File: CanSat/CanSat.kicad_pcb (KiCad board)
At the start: 2 copper layers, 7 parts, among them J1 MPU_XH2.54_M, J2 MPU_XH2.54_H, U1 ESP32_DevKit_V1, U2 LoRa Ra-02, U3 NEO6MV2 GPS, U4 MPU-6050, U5 BME280

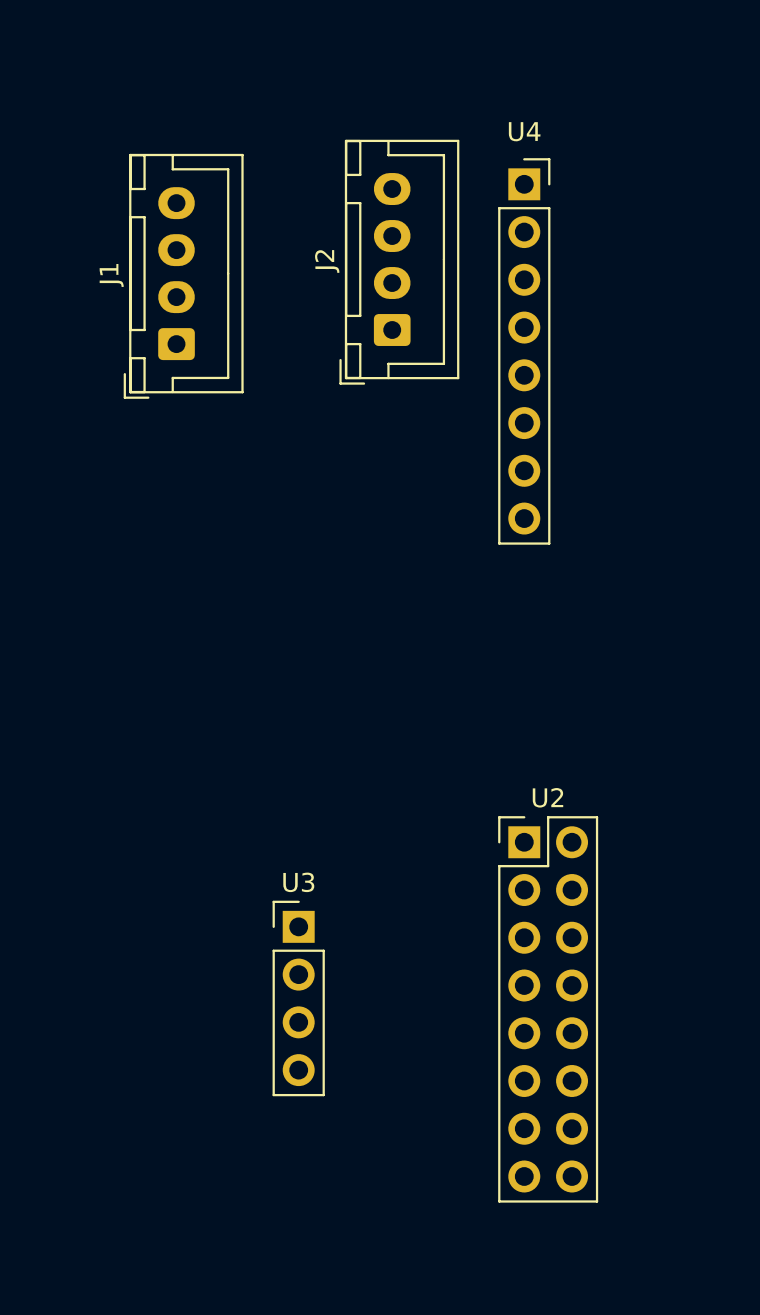
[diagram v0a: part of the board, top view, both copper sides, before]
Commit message: Updated schematic and added footprints
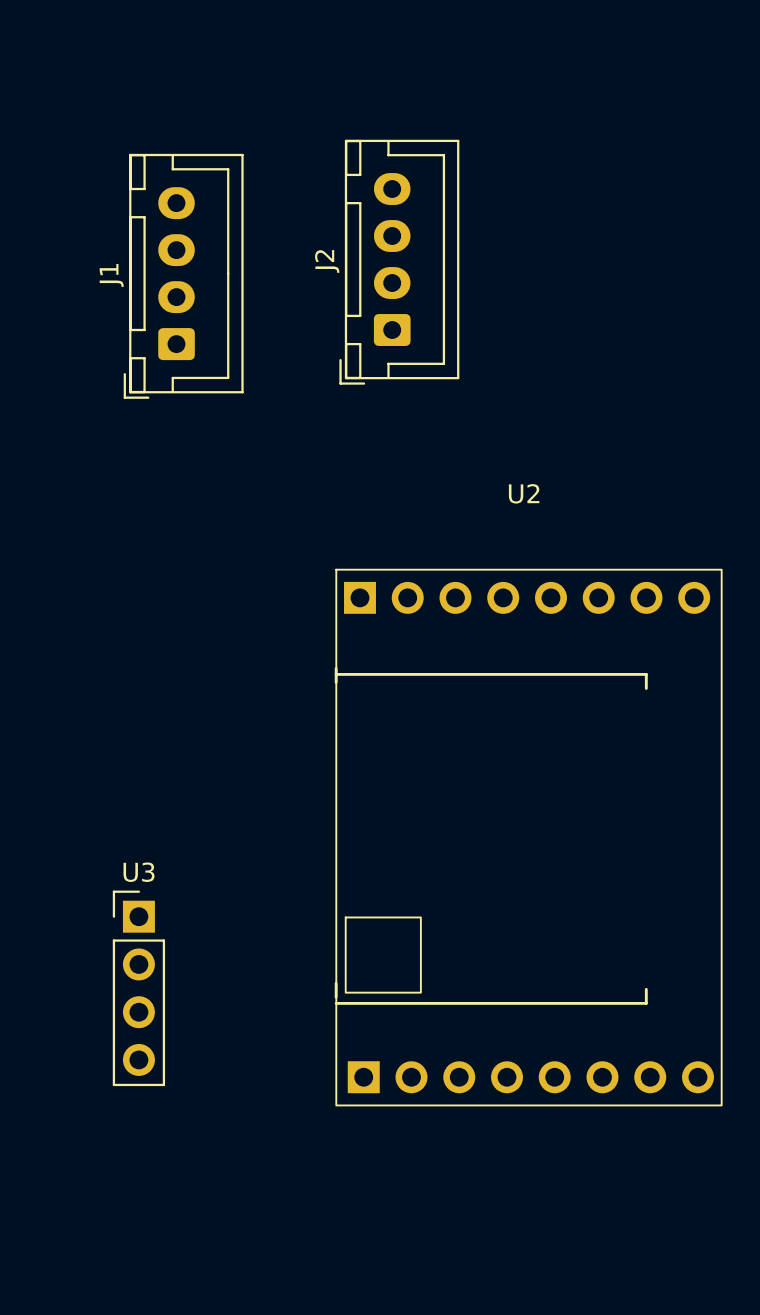
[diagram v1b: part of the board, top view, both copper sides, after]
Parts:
- removed U4: MPU-6050, Connector_PinSocket_2.54mm:PinSocket_1x08_P2.54mm_Vertical
- U2: footprint Connector_PinHeader_2.54mm:PinHeader_2x08_P2.54mm_Vertical -> MyLibrary:LoRa Ra-02
- moved U3 8.52 mm to (244.0, 120.0)

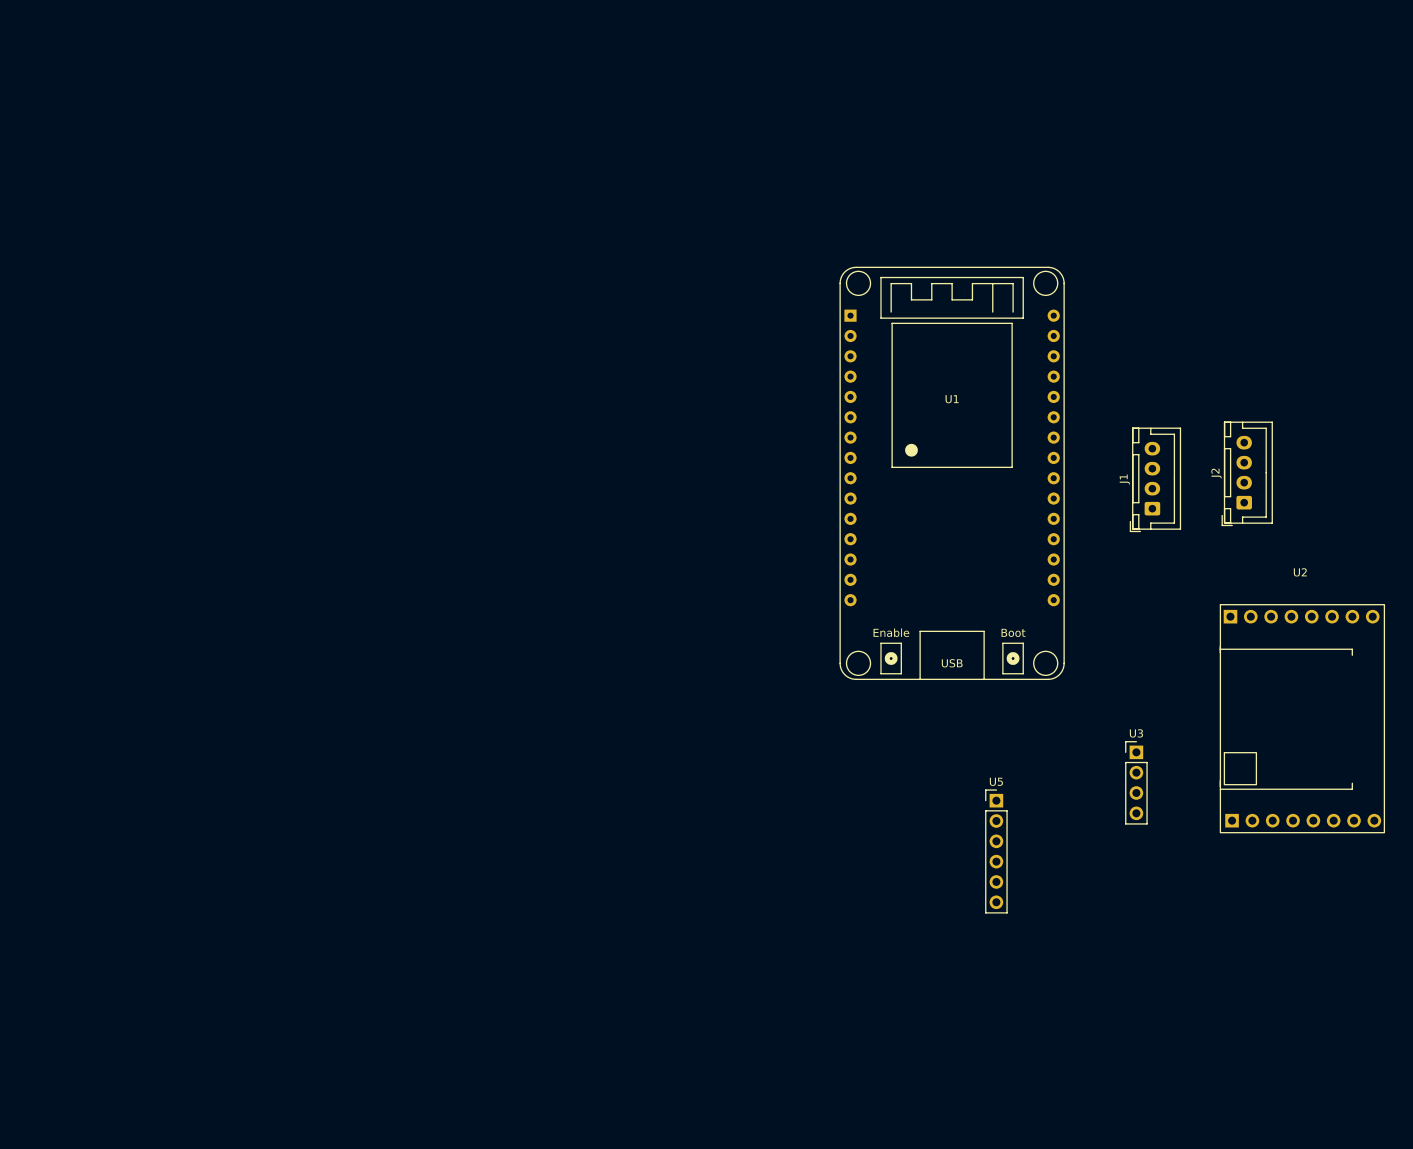
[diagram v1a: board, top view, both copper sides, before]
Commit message: Change schemes and footprints
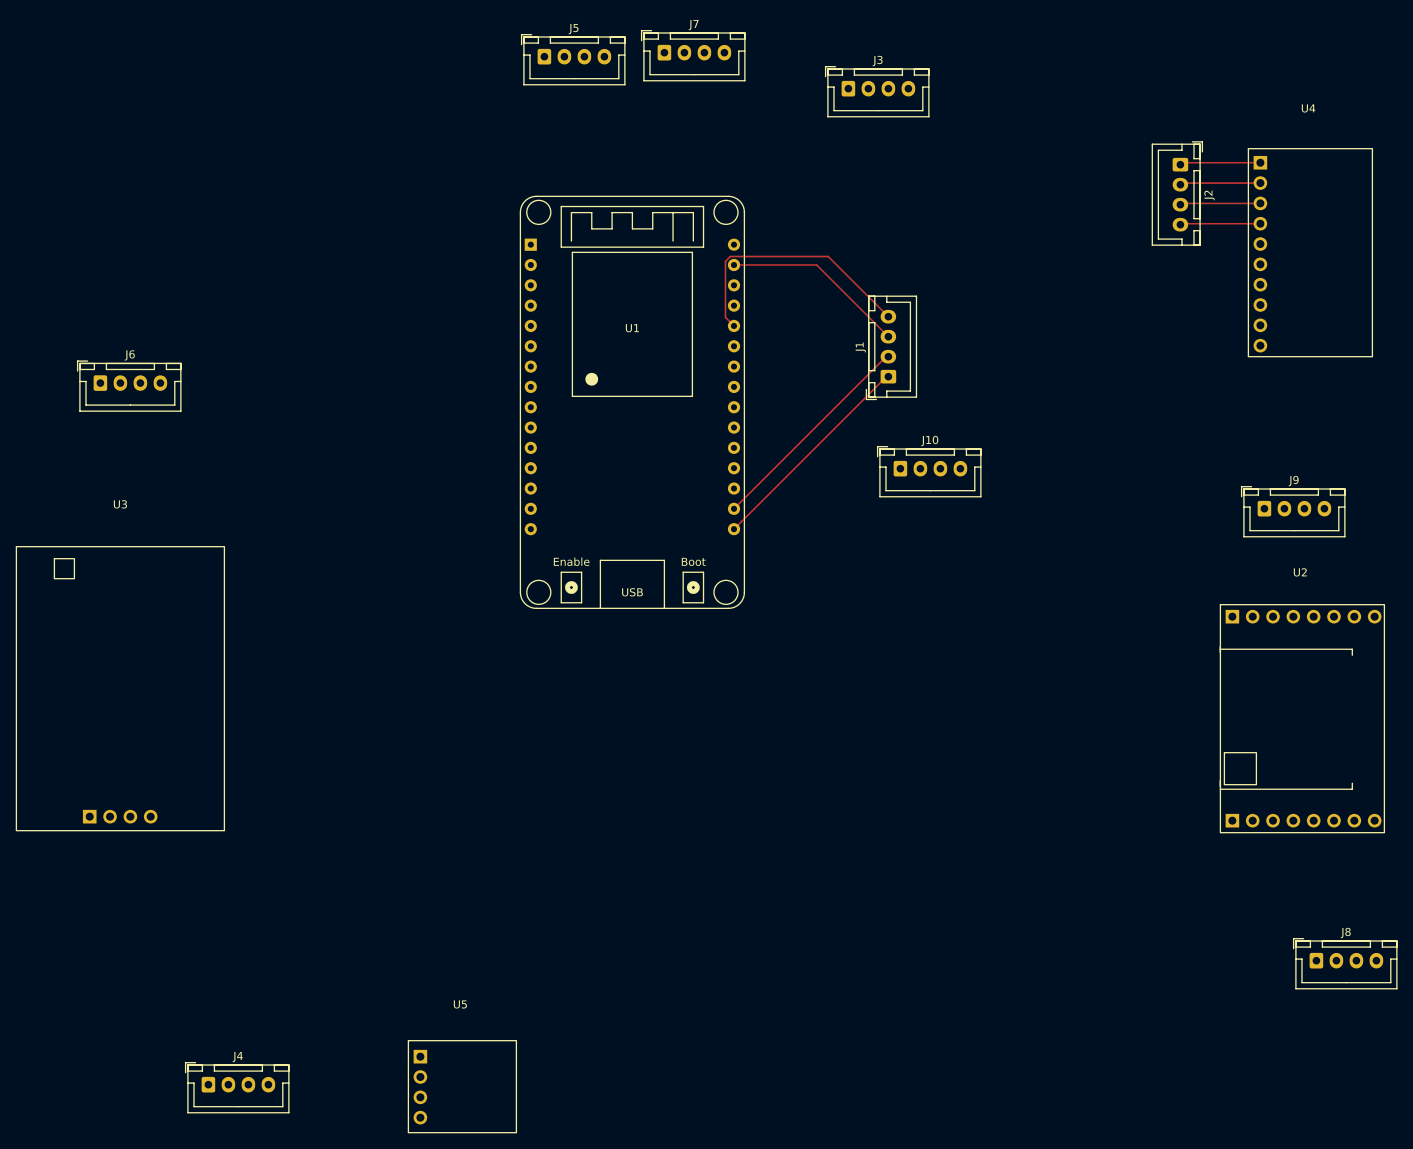
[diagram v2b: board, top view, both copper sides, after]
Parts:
- added J10: MPU_XH2.54_H, Connector_JST:JST_XH_B4B-XH-A_1x04_P2.50mm_Vertical, F.Cu at (214.5, 84.5)
- added J3: BME_XH2.54_M, Connector_JST:JST_XH_B4B-XH-A_1x04_P2.50mm_Vertical, F.Cu at (208.0, 37.0)
- added J4: BME_XH2.54_H, Connector_JST:JST_XH_B4B-XH-A_1x04_P2.50mm_Vertical, F.Cu at (128.0, 161.5)
- added J5: GPS_XH2.54_M, Connector_JST:JST_XH_B4B-XH-A_1x04_P2.50mm_Vertical, F.Cu at (170.0, 33.0)
- added J6: GPS_XH2.54_H, Connector_JST:JST_XH_B4B-XH-A_1x04_P2.50mm_Vertical, F.Cu at (114.5, 73.8)
- added J7: LoRa1_XH2.54_M, Connector_JST:JST_XH_B4B-XH-A_1x04_P2.50mm_Vertical, F.Cu at (185.0, 32.5)
- added J8: LoRa1_XH2.54_H, Connector_JST:JST_XH_B4B-XH-A_1x04_P2.50mm_Vertical, F.Cu at (266.5, 146.0)
- added J9: MPU_XH2.54_M, Connector_JST:JST_XH_B4B-XH-A_1x04_P2.50mm_Vertical, F.Cu at (260.0, 89.5)
- added U4: MPU-6500, MyLibrary:MPU-6500, F.Cu at (265.5, 57.5)
- U3: footprint Connector_PinHeader_2.54mm:PinHeader_1x04_P2.54mm_Vertical -> MyLibrary:NE06MV2 GPS
- U5: footprint Connector_PinHeader_2.54mm:PinHeader_1x06_P2.54mm_Vertical -> MyLibrary:BME280
- moved U3 127.2 mm to (117.0, 112.0)
- moved U5 76.1 mm to (159.5, 162.0)
- moved J2 43.0 mm to (249.5, 46.5), turned to -90 degrees
- moved U1 40.9 mm to (181.0, 56.5)
- moved J1 36.9 mm to (213.0, 73.0)
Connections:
- J1 pad 1: MPU.SDA -> GPS.VCC
- J1 pad 2: MPU.SCL -> GPS.GND
- J1 pad 3: MPU.GND -> BME.SCL
- J1 pad 4: MPU.VCC -> BME.SDA
- J2 pad 1: MPU.SDA -> Net-(J2-Pin_1)
- J2 pad 2: MPU.SCL -> Net-(J2-Pin_2)
- J2 pad 3: MPU.GND -> Net-(J2-Pin_3)
- J2 pad 4: MPU.VCC -> Net-(J2-Pin_4)
- U1 pad 11: unconnected-(U1-IO14-Pad11) -> LoRa1.RST
- U1 pad 16: MPU.VCC -> GPS.VCC
- U1 pad 17: MPU.GND -> GPS.GND
- U1 pad 19: unconnected-(U1-IO2-Pad19) -> LoRa1.DI00
- U1 pad 23: unconnected-(U1-IO5-Pad23) -> LoRa2.NSS
- U1 pad 24: unconnected-(U1-IO18-Pad24) -> LoRa2.SCK
- U1 pad 25: unconnected-(U1-IO19-Pad25) -> LoRa2.MISO
- U1 pad 26: MPU.SDA -> BME.SDA
- U1 pad 27: unconnected-(U1-RXD0/IO3-Pad27) -> GPS.RX
- U1 pad 28: unconnected-(U1-TXD0/IO1-Pad28) -> GPS.TX
- U1 pad 29: MPU.SCL -> BME.SCL
- U1 pad 30: unconnected-(U1-IO23-Pad30) -> LoRa2.MOSI
- U2 pad 10: LoRa2.NSS -> Net-(J9-Pin_1)
- U2 pad 11: LoRa2.MISO -> Net-(J9-Pin_2)
- U2 pad 12: LoRa2.MISO -> Net-(J9-Pin_3)
- U2 pad 13: LoRa2.SCK -> Net-(J9-Pin_4)
- U2 pad 2: LoRa1.GND -> Net-(J8-Pin_1)
- U2 pad 3: LoRa1.3.3V -> Net-(J8-Pin_2)
- U2 pad 4: LoRa1.RST -> Net-(J8-Pin_3)
- U2 pad 5: LoRa1.DI00 -> Net-(J8-Pin_4)
- U3 pad 1: GPS.GND -> Net-(J6-Pin_1)
- U3 pad 2: GPS.TX -> Net-(J6-Pin_2)
- U3 pad 3: GPS.TX -> Net-(J6-Pin_3)
- U3 pad 4: GPS.VCC -> Net-(J6-Pin_4)
- U5 pad 1: BME.GND -> Net-(J4-Pin_1)
- U5 pad 2: unconnected-(U5-CSB-Pad2) -> Net-(J4-Pin_2)
- U5 pad 3: BME.SDI -> Net-(J4-Pin_3)
- U5 pad 4: BME.SCK -> Net-(J4-Pin_4)
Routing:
- net BME.SDA: track 0.00 -> 32.2 mm
- net GPS.VCC: track 0.00 -> 27.2 mm
- net GPS.GND: track 0.00 -> 27.2 mm
- net BME.SCL: track 0.00 -> 23.0 mm
- net Net-(J2-Pin_1): track 0.00 -> 10.1 mm
- net Net-(J2-Pin_2): track 0.00 -> 10.1 mm
- net Net-(J2-Pin_3): track 0.00 -> 10.1 mm
- net Net-(J2-Pin_4): track 0.00 -> 10.0 mm

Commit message: PCBv1
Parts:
- added D1: LED_Testigo, Connector_JST:JST_XH_B2B-XH-A_1x02_P2.50mm_Vertical, F.Cu at (39.9, 42.4)
- added J11: Battery_XH2.54_M, Connector_JST:JST_XH_B2B-XH-A_1x02_P2.50mm_Vertical, F.Cu at (20.1, 42.5)
- added J12: Battery_XH2.54_H, Connector_JST:JST_XH_B2B-XH-A_1x02_P2.50mm_Vertical, F.Cu at (17.5, 97.3)
- added J13: BatteryI2C_XH2.54_M, Connector_JST:JST_XH_B2B-XH-A_1x02_P2.50mm_Vertical, F.Cu at (49.6, 42.4)
- added J14: BatteryI2C_XH2.54_H, Connector_JST:JST_XH_B2B-XH-A_1x02_P2.50mm_Vertical, F.Cu at (60.7, 76.8)
- added R1: R_330Ohm, Resistor_THT:R_Axial_DIN0207_L6.3mm_D2.5mm_P7.62mm_Horizontal, F.Cu at (28.9, 35.9)
- added SW1: SW_Power, Connector_JST:JST_XH_B2B-XH-A_1x02_P2.50mm_Vertical, F.Cu at (29.9, 42.4)
- added U6: LiPoBoostI2C, MyLibrary:LiPoBoostI2C, F.Cu at (38.1, 24.9)
- J10: value MPU_XH2.54_H -> LoRa2_XH2.54_H
- J9: value MPU_XH2.54_M -> LoRa2_XH2.54_M
- moved J10 197.3 mm to (17.5, 74.3), turned to 90 degrees
- moved J7 176.6 mm to (17.5, 88.3), turned to 90 degrees
- moved U2 174.3 mm to (100.0, 58.3)
- moved J8 172.7 mm to (116.0, 61.3), turned to -90 degrees
- moved U4 161.7 mm to (106.0, 84.3), turned to 90 degrees
- moved J2 156.3 mm to (101.5, 96.8), turned to 0 degrees
- moved J3 150.7 mm to (65.7, 86.8), turned to 180 degrees
- moved J9 149.2 mm to (115.0, 54.3), turned to 90 degrees
- moved J1 148.9 mm to (66.0, 96.8), turned to 180 degrees
- moved U1 142.5 mm to (38.5, 54.6)
- moved U5 112.0 mm to (77.8, 85.3), turned to 90 degrees
- moved J5 109.8 mm to (65.7, 67.3), turned to 180 degrees
- moved U3 87.8 mm to (93.5, 27.4), turned to 90 degrees
- moved J4 83.4 mm to (75.3, 96.8)
- moved J6 43.4 mm to (115.0, 30.4), turned to 90 degrees
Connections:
- net BME.SCL renamed MPU.SCL
- net BME.SDA renamed MPU.SDA
- J1 pad 1: GPS.VCC -> MPU.VCC
- J1 pad 2: GPS.GND -> MPU.GND
- J10 pad 2: LoRa2.MISO -> LoRa2.SCK
- J10 pad 4: LoRa2.SCK -> LoRa2.MOSI
- J3 pad 1: GPS.VCC -> MPU.VCC
- J3 pad 2: GPS.GND -> MPU.GND
- J5 pad 1: GPS.GND -> MPU.VCC
- J5 pad 2: GPS.TX -> MPU.GND
- J5 pad 4: GPS.VCC -> GPS.RX
- J7 pad 1: GPS.GND -> MPU.VCC
- J7 pad 2: GPS.VCC -> MPU.GND
- U1 pad 14: unconnected-(U1-GND-Pad14) -> Net-(J12-Pin_1)
- U1 pad 15: unconnected-(U1-VIN-Pad15) -> Net-(J12-Pin_2)
- U1 pad 16: GPS.VCC -> MPU.VCC
- U1 pad 17: GPS.GND -> MPU.GND
- U2 pad 11: Net-(J9-Pin_2) -> Net-(J9-Pin_4)
- U2 pad 13: Net-(J9-Pin_4) -> Net-(J9-Pin_2)
- U2 pad 2: Net-(J8-Pin_1) -> Net-(J8-Pin_2)
- U2 pad 3: Net-(J8-Pin_2) -> Net-(J8-Pin_1)
- U3 pad 1: Net-(J6-Pin_1) -> Net-(J6-Pin_2)
- U3 pad 2: Net-(J6-Pin_2) -> Net-(J6-Pin_3)
- U3 pad 3: Net-(J6-Pin_3) -> Net-(J6-Pin_4)
- U3 pad 4: Net-(J6-Pin_4) -> Net-(J6-Pin_1)
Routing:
- net MPU.VCC: track 0.00 -> 88.0 mm
- net MPU.GND: track 0.00 -> 86.4 mm
- net Net-(J13-Pin_1): track 0.00 -> 39.0 mm
- net LoRa2.MOSI: track 0.00 -> 38.8 mm
- net LoRa1.DI00: track 0.00 -> 36.1 mm
- net LoRa2.MISO: track 0.00 -> 34.5 mm
- net LoRa2.SCK: track 0.00 -> 34.5 mm
- net LoRa2.NSS: track 0.00 -> 34.5 mm
- net Net-(J11-Pin_1): track 0.00 -> 33.9 mm
- net Net-(J13-Pin_2): track 0.00 -> 32.6 mm
- net Net-(J8-Pin_1): track 0.00 -> 27.2 mm
- net GPS.VCC: track 27.2 -> 0.00 mm
- net GPS.GND: track 27.2 -> 0.00 mm
- net Net-(J8-Pin_2): track 0.00 -> 25.7 mm
- net Net-(J9-Pin_1): track 0.00 -> 24.7 mm
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
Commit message: Beta version 1.0
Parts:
- moved U5 101.3 mm to (166.4, 134.5), turned to -90 degrees
- moved U3 99.4 mm to (183.0, 70.4), turned to -90 degrees
- moved U4 97.1 mm to (188.5, 135.6), turned to -90 degrees
- moved J4 97.1 mm to (168.9, 123.0), turned to 180 degrees
- moved J2 95.2 mm to (193.0, 123.1), turned to 180 degrees
- moved J1 95.1 mm to (150.5, 140.5)
- moved J10 95.1 mm to (102.0, 118.0)
- moved J12 95.1 mm to (102.0, 141.0)
- moved J14 95.1 mm to (145.2, 120.5)
- moved J3 95.1 mm to (150.2, 130.5)
- moved J5 95.1 mm to (150.2, 111.0)
- moved J7 95.1 mm to (102.0, 132.0)
- moved U1 95.1 mm to (123.0, 98.3)
- moved J13 94.7 mm to (134.1, 85.1)
- moved U6 94.7 mm to (122.6, 67.6)
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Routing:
- net Net-(J8-Pin_1): track 27.2 -> 28.2 mm
- net Net-(J9-Pin_2): track 19.9 -> 20.7 mm
